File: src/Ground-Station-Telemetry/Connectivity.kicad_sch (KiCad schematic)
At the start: 11 parts, among them P2 USB, U3 CP2102-GMR(QFN28), U4 RFM95W-868S2, U5 XB24CDMPIT-001

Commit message: routed rev1
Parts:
- renumbered D3 to D4, R7 to R8, R8 to R9
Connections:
- net D+: now also D4.3; no longer D4.1
- net D-: now also D4.1; no longer D4.3
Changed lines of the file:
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@@
   (junction (at 47.625 63.5) (diameter 0) (color 0 0 0 0)
   )
-  (junction (at 59.055 54.61) (diameter 0) (color 0 0 0 0)
-  )
   (junction (at 47.625 60.96) (diameter 0) (color 0 0 0 0)
   )
-  (junction (at 66.675 52.07) (diameter 0) (color 0 0 0 0)
-  )
   (junction (at 99.695 70.485) (diameter 0) (color 0 0 0 0)
   )
@@
   (junction (at 246.38 69.85) (diameter 0) (color 0 0 0 0)
   )
+  (junction (at 66.675 54.61) (diameter 0) (color 0 0 0 0)
+  )
   (junction (at 73.66 49.53) (diameter 0) (color 0 0 0 0)
+  )
+  (junction (at 59.055 52.07) (diameter 0) (color 0 0 0 0)
   )
   (no_connect (at 134.62 72.39))
@@
     (stroke (width 0) (type default) (color 0 0 0 0))
   )
-  (wire (pts (xy 45.72 52.07) (xy 66.675 52.07))
+  (wire (pts (xy 45.72 52.07) (xy 59.055 52.07))
     (stroke (width 0) (type default) (color 0 0 0 0))
   )
@@
     (stroke (width 0) (type default) (color 0 0 0 0))
   )
-  (wire (pts (xy 66.675 52.07) (xy 66.675 60.325))
-    (stroke (width 0) (type default) (color 0 0 0 0))
-  )
   (wire (pts (xy 241.935 124.46) (xy 245.11 124.46))
     (stroke (width 0) (type default) (color 0 0 0 0))
@@
     (stroke (width 0) (type default) (color 0 0 0 0))
   )
-  (wire (pts (xy 45.72 54.61) (xy 59.055 54.61))
-    (stroke (width 0) (type default) (color 0 0 0 0))
-  )
   (wire (pts (xy 208.28 139.7) (xy 211.455 139.7))
     (stroke (width 0) (type default) (color 0 0 0 0))
@@
     (stroke (width 0) (type default) (color 0 0 0 0))
   )
-  (wire (pts (xy 59.055 54.61) (xy 59.055 60.325))
-    (stroke (width 0) (type default) (color 0 0 0 0))
-  )
   (wire (pts (xy 208.28 134.62) (xy 211.455 134.62))
     (stroke (width 0) (type default) (color 0 0 0 0))
@@
     (stroke (width 0) (type default) (color 0 0 0 0))
   )
+  (wire (pts (xy 66.675 54.61) (xy 66.675 60.325))
+    (stroke (width 0) (type default) (color 0 0 0 0))
+  )
   (wire (pts (xy 243.205 69.85) (xy 246.38 69.85))
     (stroke (width 0) (type default) (color 0 0 0 0))
@@
     (stroke (width 0) (type default) (color 0 0 0 0))
   )
-  (wire (pts (xy 66.675 52.07) (xy 116.84 52.07))
-    (stroke (width 0) (type default) (color 0 0 0 0))
-  )
   (wire (pts (xy 93.98 70.485) (xy 99.695 70.485))
     (stroke (width 0) (type default) (color 0 0 0 0))
@@
     (stroke (width 0) (type default) (color 0 0 0 0))
   )
+  (wire (pts (xy 59.055 52.07) (xy 116.84 52.07))
+    (stroke (width 0) (type default) (color 0 0 0 0))
+  )
   (polyline (pts (xy 19.05 17.145) (xy 167.64 17.145))
     (stroke (width 0) (type default) (color 0 0 0 0))
@@
     (stroke (width 0) (type default) (color 0 0 0 0))
   )
-  (wire (pts (xy 59.055 54.61) (xy 116.84 54.61))
+  (wire (pts (xy 45.72 54.61) (xy 66.675 54.61))
     (stroke (width 0) (type default) (color 0 0 0 0))
   )
@@
     (stroke (width 0) (type default) (color 0 0 0 0))
   )
+  (wire (pts (xy 66.675 54.61) (xy 116.84 54.61))
+    (stroke (width 0) (type default) (color 0 0 0 0))
+  )
   (polyline (pts (xy 170.815 17.145) (xy 172.72 17.145))
     (stroke (width 0) (type default) (color 0 0 0 0))
@@
   )
   (wire (pts (xy 104.14 59.69) (xy 104.14 61.595))
+    (stroke (width 0) (type default) (color 0 0 0 0))
+  )
+  (wire (pts (xy 59.055 52.07) (xy 59.055 60.325))
     (stroke (width 0) (type default) (color 0 0 0 0))
   )
@@
   (symbol (lib_id "Ground-Station-Telemetry:Earth") (at 113.03 56.515 0) (unit 1)
     (in_bom yes) (on_board yes) (fields_autoplaced)
-    (property "Reference" "#PWR016" (id 0) (at 113.03 62.865 0)
+    (property "Reference" "#PWR017" (id 0) (at 113.03 62.865 0)
       (effects (font (size 1.27 1.27)) hide)
     )
@@
   (symbol (lib_id "Ground-Station-Telemetry:Earth") (at 69.85 73.025 0) (unit 1)
     (in_bom yes) (on_board yes) (fields_autoplaced)
-    (property "Reference" "#PWR014" (id 0) (at 69.85 79.375 0)
+    (property "Reference" "#PWR015" (id 0) (at 69.85 79.375 0)
       (effects (font (size 1.27 1.27)) hide)
     )
@@
   (symbol (lib_id "Ground-Station-Telemetry:Earth") (at 264.795 58.42 0) (unit 1)
     (in_bom yes) (on_board yes) (fields_autoplaced)
-    (property "Reference" "#PWR022" (id 0) (at 264.795 64.77 0)
+    (property "Reference" "#PWR023" (id 0) (at 264.795 64.77 0)
       (effects (font (size 1.27 1.27)) hide)
     )
@@
   (symbol (lib_id "Ground-Station-Telemetry:Earth") (at 137.16 90.805 0) (unit 1)
     (in_bom yes) (on_board yes) (fields_autoplaced)
-    (property "Reference" "#PWR017" (id 0) (at 137.16 97.155 0)
+    (property "Reference" "#PWR018" (id 0) (at 137.16 97.155 0)
       (effects (font (size 1.27 1.27)) hide)
     )
@@
   (symbol (lib_id "Ground-Station-Telemetry:Earth") (at 210.185 148.59 0) (unit 1)
     (in_bom yes) (on_board yes) (fields_autoplaced)
-    (property "Reference" "#PWR019" (id 0) (at 210.185 154.94 0)
+    (property "Reference" "#PWR020" (id 0) (at 210.185 154.94 0)
       (effects (font (size 1.27 1.27)) hide)
     )
@@
   (symbol (lib_id "Ground-Station-Telemetry:RES_0603") (at 132.08 85.725 90) (unit 1)
     (in_bom yes) (on_board yes)
-    (property "Reference" "R7" (id 0) (at 128.27 84.455 90)
+    (property "Reference" "R8" (id 0) (at 128.27 84.455 90)
       (effects (font (size 1.27 1.27)) (justify right))
     )
@@
   (symbol (lib_id "Ground-Station-Telemetry:RES_0603") (at 137.16 85.725 90) (unit 1)
     (in_bom yes) (on_board yes) (fields_autoplaced)
-    (property "Reference" "R8" (id 0) (at 138.9126 84.8903 90)
+    (property "Reference" "R9" (id 0) (at 138.9126 84.8903 90)
       (effects (font (size 1.27 1.27)) (justify right))
     )
@@
   (symbol (lib_id "Ground-Station-Telemetry:Earth") (at 47.625 65.405 0) (unit 1)
     (in_bom yes) (on_board yes) (fields_autoplaced)
-    (property "Reference" "#PWR013" (id 0) (at 47.625 71.755 0)
+    (property "Reference" "#PWR014" (id 0) (at 47.625 71.755 0)
       (effects (font (size 1.27 1.27)) hide)
     )
@@
   (symbol (lib_id "Ground-Station-Telemetry:Earth") (at 248.92 55.245 0) (unit 1)
     (in_bom yes) (on_board yes) (fields_autoplaced)
-    (property "Reference" "#PWR021" (id 0) (at 248.92 61.595 0)
+    (property "Reference" "#PWR022" (id 0) (at 248.92 61.595 0)
       (effects (font (size 1.27 1.27)) hide)
     )
@@
   (symbol (lib_id "Ground-Station-Telemetry:SP0504BAHTG") (at 69.85 66.04 0) (unit 1)
     (in_bom yes) (on_board yes) (fields_autoplaced)
-    (property "Reference" "D3" (id 0) (at 54.9148 66.1795 0)
+    (property "Reference" "D4" (id 0) (at 54.9148 66.1795 0)
       (effects (font (size 1.524 1.524)) (justify right))
     )
@@
   (symbol (lib_id "Ground-Station-Telemetry:Earth") (at 99.695 71.755 0) (unit 1)
     (in_bom yes) (on_board yes) (fields_autoplaced)
-    (property "Reference" "#PWR015" (id 0) (at 99.695 78.105 0)
+    (property "Reference" "#PWR016" (id 0) (at 99.695 78.105 0)
       (effects (font (size 1.27 1.27)) hide)
     )
@@
   (symbol (lib_id "Ground-Station-Telemetry:Earth") (at 153.035 73.66 0) (unit 1)
     (in_bom yes) (on_board yes) (fields_autoplaced)
-    (property "Reference" "#PWR018" (id 0) (at 153.035 80.01 0)
+    (property "Reference" "#PWR019" (id 0) (at 153.035 80.01 0)
       (effects (font (size 1.27 1.27)) hide)
     )
@@
   (symbol (lib_id "Ground-Station-Telemetry:Earth") (at 246.38 71.12 0) (unit 1)
     (in_bom yes) (on_board yes) (fields_autoplaced)
-    (property "Reference" "#PWR020" (id 0) (at 246.38 77.47 0)
-      (effects (font (size 1.27 1.27)) hide)
-    )
+    (property "Reference" "#PWR021" (id 0) (at 246.38 77.47 0)
+      (effects (font (size 1.27 1.27)) hide)
+    )

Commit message: added RS485 transceiver to schematic
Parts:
- added C1: 0.1uF, Ground-Station-Telemetry:CAP_0603, symbol Ground-Station-Telemetry:CAP_0603
- added D2, D3: SMBJ36CA-13-F, Ground-Station-Telemetry:CDSOT23-SM712, symbol RS485-Module:CDSOT23-SM712
- added P3: 54602-908LF, Ground-Station-Telemetry:54602-908LF, symbol Ground-Station-Telemetry:54602-908LF
- added R2, R3, R4, R5: 10, Ground-Station-Telemetry:RES_0603, symbol RS485-Module:RES_0603
- added R6, R7: 100, Ground-Station-Telemetry:RES_0603, symbol RS485-Module:RES_0603
- added U1: SN65HVD71DR, Ground-Station-Telemetry:SN65HVD71DR, symbol RS485-Module:SN65HVD71DR
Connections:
- net 3.3V: now also C1.1, U1.1 (VCC)
- net Earth: now also C1.2, D2.3, D3.3, U1.4 (GND)
- new net: R5.1, U1.5 (Y)
- new net: R4.1, U1.6 (Z)
- new net: R3.1, U1.7 (B)
- new net: R2.1, U1.8 (A)
- new net A: D2.1, P3.2, R2.2, R6.2
- new net B: D2.2, P3.1, R3.2, R6.1
- new net RS485_RX: U1.2 (R)
- new net RS485_TX: U1.3 (D)
- new net Y: D3.2, P3.8, R5.2, R7.1
- new net Z: D3.1, P3.7, R4.2, R7.2
- no-connect marks 22 -> 26
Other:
- note added: "RJ45 Connector: CAT6 UTP, Straight Through T-568B"
- note added: "RS485 Transceiver"

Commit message: finished initial rev 2 routing
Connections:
- net 5V: now also D4.5; no longer D4.4
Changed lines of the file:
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@@
   (junction (at 99.695 70.485) (diameter 0) (color 0 0 0 0)
   )
+  (junction (at 58.928 52.07) (diameter 0) (color 0 0 0 0)
+  )
+  (junction (at 80.518 49.53) (diameter 0) (color 0 0 0 0)
+  )
   (junction (at 248.92 44.45) (diameter 0) (color 0 0 0 0)
   )
@@
   (junction (at 88.392 136.906) (diameter 0) (color 0 0 0 0)
   )
+  (junction (at 66.548 54.61) (diameter 0) (color 0 0 0 0)
+  )
   (junction (at 117.856 130.302) (diameter 0) (color 0 0 0 0)
   )
   (junction (at 246.38 69.85) (diameter 0) (color 0 0 0 0)
   )
-  (junction (at 66.675 54.61) (diameter 0) (color 0 0 0 0)
-  )
-  (junction (at 73.66 49.53) (diameter 0) (color 0 0 0 0)
-  )
   (junction (at 103.124 124.714) (diameter 0) (color 0 0 0 0)
-  )
-  (junction (at 59.055 52.07) (diameter 0) (color 0 0 0 0)
   )
   (no_connect (at 148.59 139.7))
@@
   (no_connect (at 241.935 139.7))
   (no_connect (at 116.84 57.15))
-  (no_connect (at 80.645 60.325))
   (no_connect (at 148.59 127))
   (no_connect (at 148.59 137.16))
@@
   (no_connect (at 144.78 31.75))
   (no_connect (at 129.54 31.75))
+  (no_connect (at 73.66 60.198))
   (no_connect (at 211.455 142.24))
   (wire (pts (xy 204.47 52.07) (xy 207.645 52.07))
@@
     (stroke (width 0) (type default))
   )
-  (wire (pts (xy 69.85 71.755) (xy 69.85 73.025))
-    (stroke (width 0) (type default))
-  )
   (wire (pts (xy 204.47 69.85) (xy 207.645 69.85))
     (stroke (width 0) (type default))
@@
     (stroke (width 0) (type default))
   )
-  (wire (pts (xy 45.72 52.07) (xy 59.055 52.07))
+  (wire (pts (xy 45.72 52.07) (xy 58.928 52.07))
     (stroke (width 0) (type default))
   )
@@
     (stroke (width 0) (type default))
   )
+  (wire (pts (xy 80.518 49.53) (xy 89.662 49.53))
+    (stroke (width 0) (type default))
+  )
   (polyline (pts (xy 170.815 99.695) (xy 170.815 17.145))
     (stroke (width 0) (type default))
@@
     (stroke (width 0) (type default))
   )
-  (wire (pts (xy 73.66 49.53) (xy 76.2 49.53))
+  (wire (pts (xy 45.72 49.53) (xy 80.518 49.53))
     (stroke (width 0) (type default))
   )
@@
     (stroke (width 0) (type default))
   )
-  (wire (pts (xy 66.675 54.61) (xy 66.675 60.325))
-    (stroke (width 0) (type default))
-  )
   (wire (pts (xy 95.504 127.508) (xy 124.968 127.508))
     (stroke (width 0) (type default))
@@
     (stroke (width 0) (type default))
   )
+  (wire (pts (xy 58.928 52.07) (xy 116.84 52.07))
+    (stroke (width 0) (type default))
+  )
   (wire (pts (xy 110.236 121.92) (xy 127.762 121.92))
     (stroke (width 0) (type default))
@@
     (stroke (width 0) (type default))
   )
+  (wire (pts (xy 69.85 71.628) (xy 69.85 73.152))
+    (stroke (width 0) (type default))
+  )
   (wire (pts (xy 88.392 131.826) (xy 88.392 131.064))
     (stroke (width 0) (type default))
@@
     (stroke (width 0) (type default))
   )
+  (wire (pts (xy 58.928 52.07) (xy 58.928 60.198))
+    (stroke (width 0) (type default))
+  )
   (wire (pts (xy 243.205 67.31) (xy 246.38 67.31))
     (stroke (width 0) (type default))
@@
     (stroke (width 0) (type default))
   )
-  (wire (pts (xy 59.055 52.07) (xy 116.84 52.07))
+  (wire (pts (xy 66.548 54.61) (xy 66.548 60.198))
     (stroke (width 0) (type default))
   )
@@
     (stroke (width 0) (type default))
   )
-  (wire (pts (xy 45.72 54.61) (xy 66.675 54.61))
+  (wire (pts (xy 45.72 54.61) (xy 66.548 54.61))
     (stroke (width 0) (type default))
   )
@@
     (stroke (width 0) (type default))
   )
-  (wire (pts (xy 66.675 54.61) (xy 116.84 54.61))
-    (stroke (width 0) (type default))
-  )
   (polyline (pts (xy 170.815 17.145) (xy 172.72 17.145))
     (stroke (width 0) (type default))
@@
     (stroke (width 0) (type default))
   )
-  (wire (pts (xy 73.66 49.53) (xy 73.66 60.325))
-    (stroke (width 0) (type default))
-  )
-  (wire (pts (xy 45.72 49.53) (xy 73.66 49.53))
-    (stroke (width 0) (type default))
-  )
   (wire (pts (xy 208.28 144.78) (xy 211.455 144.78))
     (stroke (width 0) (type default))
   )
+  (wire (pts (xy 66.548 54.61) (xy 116.84 54.61))
+    (stroke (width 0) (type default))
+  )
   (wire (pts (xy 99.695 70.485) (xy 99.695 71.755))
     (stroke (width 0) (type default))
@@
     (stroke (width 0) (type default))
   )
+  (wire (pts (xy 80.518 49.53) (xy 80.518 60.198))
+    (stroke (width 0) (type default))
+  )
   (wire (pts (xy 144.018 134.62) (xy 148.59 134.62))
     (stroke (width 0) (type default))
@@
   )
   (wire (pts (xy 104.14 59.69) (xy 104.14 61.595))
-    (stroke (width 0) (type default))
-  )
-  (wire (pts (xy 59.055 52.07) (xy 59.055 60.325))
     (stroke (width 0) (type default))
   )
@@
     )
   )
-  (global_label "5V" (shape input) (at 76.2 49.53 0) (fields_autoplaced)
-    (effects (font (size 1.27 1.27)) (justify left))
-    (property "Intersheetrefs" "${INTERSHEET_REFS}" (at 80.9112 49.4506 0)
+  (global_label "5V" (shape input) (at 89.662 49.53 0) (fields_autoplaced)
+    (effects (font (size 1.27 1.27)) (justify left))
+    (property "Intersheetrefs" "${INTERSHEET_REFS}" (at 94.3732 49.4506 0)
       (effects (font (size 1.27 1.27)) (justify left) hide)
     )
@@
     )
   )
-  (symbol (lib_id "Ground-Station-Telemetry:Earth") (at 69.85 73.025 0) (unit 1)
+  (symbol (lib_id "Ground-Station-Telemetry:Earth") (at 69.85 73.152 0) (unit 1)
     (in_bom yes) (on_board yes) (dnp no) (fields_autoplaced)
-    (property "Reference" "#PWR015" (at 69.85 79.375 0)
+    (property "Reference" "#PWR015" (at 69.85 79.502 0)
       (effects (font (size 1.27 1.27)) hide)
     )
-    (property "Value" "Earth" (at 69.85 76.835 0)
+    (property "Value" "Earth" (at 69.85 76.962 0)
       (effects (font (size 1.27 1.27)) hide)
     )
-    (property "Footprint" "" (at 69.85 73.025 0)
+    (property "Footprint" "" (at 69.85 73.152 0)
       (effects (font (size 1.27 1.27)) hide)
     )
-    (property "Datasheet" "" (at 69.85 73.025 0)
+    (property "Datasheet" "" (at 69.85 73.152 0)
       (effects (font (size 1.27 1.27)) hide)
     )

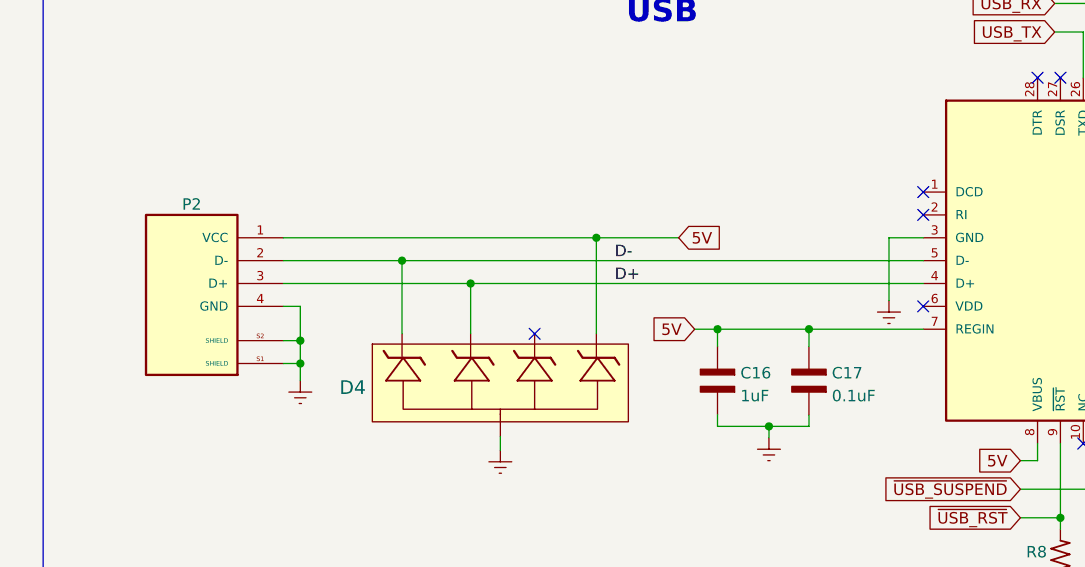
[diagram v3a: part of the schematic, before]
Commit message: added PCB images to README
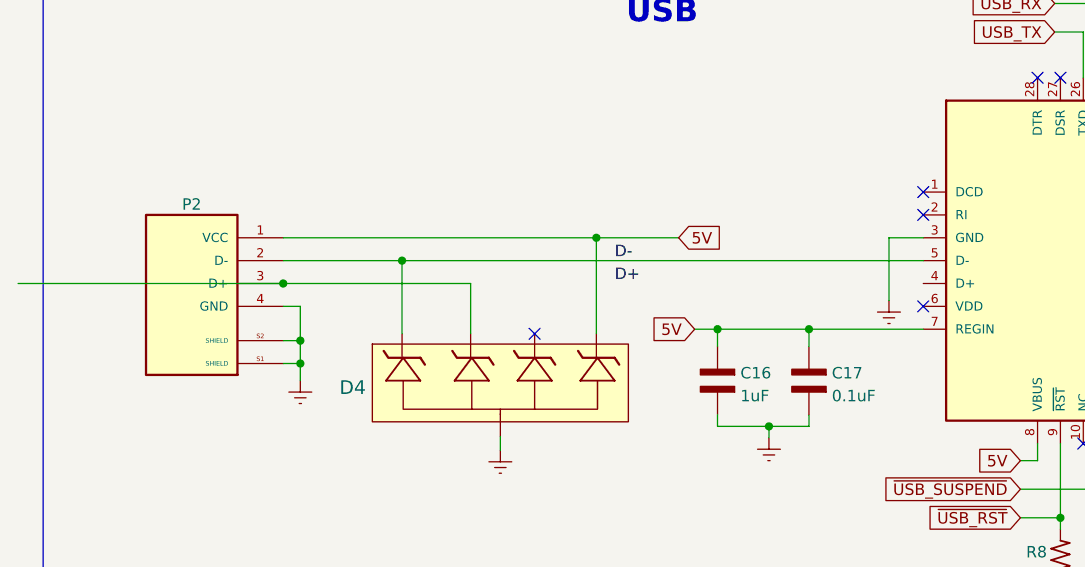
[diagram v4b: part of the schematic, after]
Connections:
- net D+: no longer D4.3, P2.3 (D+), U3.4 (D+)
- new net: D4.3, P2.3 (D+)
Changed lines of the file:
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@@
   (junction (at 58.928 52.07) (diameter 0) (color 0 0 0 0)
   )
+  (junction (at 45.72 54.61) (diameter 0) (color 0 0 0 0)
+  )
   (junction (at 80.518 49.53) (diameter 0) (color 0 0 0 0)
   )
@@
   )
   (junction (at 88.392 136.906) (diameter 0) (color 0 0 0 0)
-  )
-  (junction (at 66.548 54.61) (diameter 0) (color 0 0 0 0)
   )
   (junction (at 117.856 130.302) (diameter 0) (color 0 0 0 0)
@@
     (stroke (width 0) (type default))
   )
+  (wire (pts (xy 45.72 54.61) (xy 16.256 54.61))
+    (stroke (width 0) (type default))
+  )
   (polyline (pts (xy 172.085 17.145) (xy 280.67 17.145))
     (stroke (width 0) (type default))
@@
     (stroke (width 0) (type default))
   )
-  (wire (pts (xy 66.548 54.61) (xy 116.84 54.61))
-    (stroke (width 0) (type default))
-  )
